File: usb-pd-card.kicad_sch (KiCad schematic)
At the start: 48 parts, among them J1 USB_C_Receptacle_USB2.0_14P, U1 CH32X035G8U6, U2 HT7533-1, U3 NT3H2111W0FHKH

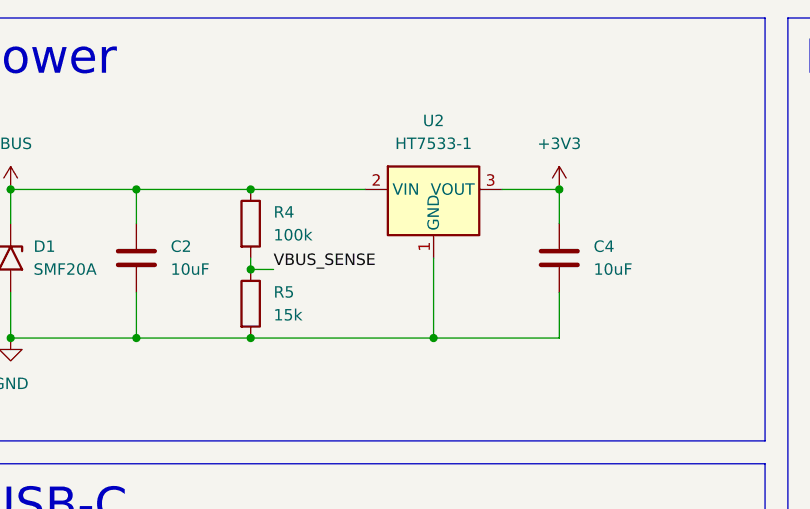
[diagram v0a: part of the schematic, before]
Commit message: v1: PCB layout complete, JLC production files
- Credit-card outline (85.6 x 53.98 mm, r3.18), USB-C paddle on the left edge
- Electronics routed, GND pour on both layers over the electronics half
- NFC coil 46 x 38 mm, 5 turns (est. 2.31 uH, f0 ~14.4 MHz), C3 DNP
- Regulator ME6228A33M3G (SOT-23-3), C2 0603, D1 SOD-123F footprint
- Contact info + QR code on the back, LED/test-pad labels on the front
- tools/nfc_coil.py coil generator and lib/nfc-coils.pretty footprint
- JLCPCB Gerbers, BOM and CPL in jlcpcb/
- README with board renders; AGENTS.md updated with final decisions
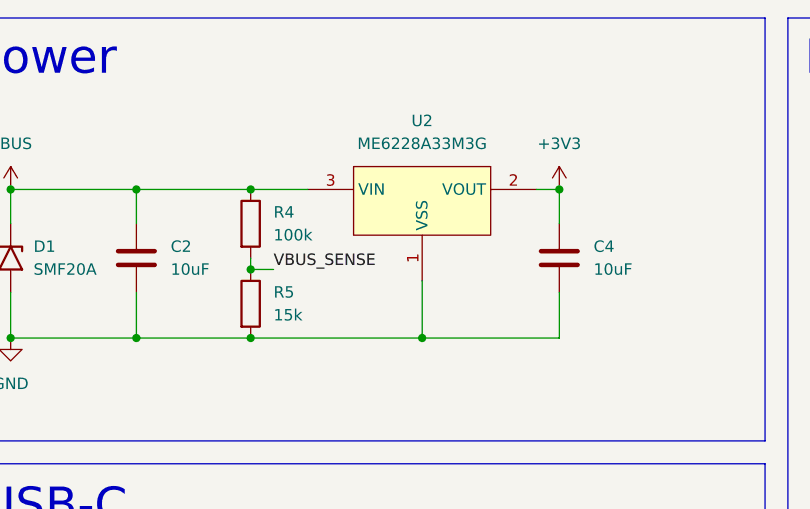
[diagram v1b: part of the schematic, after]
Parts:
- C2: footprint Capacitor_SMD:C_0805_2012Metric -> Capacitor_SMD:C_0603_1608Metric; LCSC C15850 -> C96446
- D1: footprint Diode_SMD:D_SMF -> Diode_SMD:D_SOD-123F
- L1: footprint (none) -> nfc-coils:NFC_Coil_Rect_38x46mm_R4_5T_W0.5_S0.3
- U2: value HT7533-1 -> ME6228A33M3G; footprint Package_TO_SOT_SMD:SOT-89-3 -> business-card:SOT-23-3_L2.9-W1.6-P1.90-LS2.8-BR; symbol Regulator_Linear:HT75xx-1-SOT89 -> business-card:ME6228A33M3G; LCSC C14289 -> C487914; MPN (none) -> ME6228A33M3G; Manufacturer (none) -> MICRONE(南京微盟)
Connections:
- net +3V3: now also U2.2 (VOUT); no longer U2.3 (VOUT)
- net VBUS: now also U2.3 (VIN); no longer U2.2 (VIN)
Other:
- moved on the sheet: U2
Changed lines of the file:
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@@
 	)
 	(junction
-		(at 152.4 34.29)
-		(diameter 0)
-		(color 0 0 0 0)
-	)
-	(junction
 		(at 101.6 123.19)
 		(diameter 0)
@@
 	)
 	(junction
-		(at 138.43 50.8)
+		(at 133.35 91.44)
 		(diameter 0)
 		(color 0 0 0 0)
 	)
 	(junction
-		(at 133.35 91.44)
+		(at 152.4 34.29)
 		(diameter 0)
 		(color 0 0 0 0)
@@
 	)
 	(junction
-		(at 118.11 34.29)
-		(diameter 0)
-		(color 0 0 0 0)
-	)
-	(junction
 		(at 266.7 68.58)
 		(diameter 0)
@@
 	)
 	(junction
+		(at 137.16 50.8)
+		(diameter 0)
+		(color 0 0 0 0)
+	)
+	(junction
 		(at 229.87 105.41)
 		(diameter 0)
@@
 	)
 	(junction
+		(at 118.11 34.29)
+		(diameter 0)
+		(color 0 0 0 0)
+	)
+	(junction
 		(at 123.19 91.44)
 		(diameter 0)
@@
 	(wire
 		(pts
+			(xy 118.11 34.29) (xy 124.46 34.29)
+		)
+		(stroke
+			(width 0)
+			(type default)
+		)
+	)
+	(wire
+		(pts
 			(xy 118.11 41.91) (xy 118.11 43.18)
 		)
@@
 	(wire
 		(pts
-			(xy 118.11 34.29) (xy 130.81 34.29)
+			(xy 245.11 43.18) (xy 248.92 43.18)
 		)
 		(stroke
@@
 	(wire
 		(pts
-			(xy 146.05 34.29) (xy 152.4 34.29)
+			(xy 210.82 53.34) (xy 214.63 53.34)
 		)
 		(stroke
@@
 	(wire
 		(pts
-			(xy 245.11 43.18) (xy 248.92 43.18)
+			(xy 118.11 43.18) (xy 120.65 43.18)
 		)
 		(stroke
@@
 	(wire
 		(pts
-			(xy 210.82 53.34) (xy 214.63 53.34)
+			(xy 57.15 60.96) (xy 59.69 60.96)
 		)
 		(stroke
@@
 	(wire
 		(pts
-			(xy 118.11 43.18) (xy 120.65 43.18)
+			(xy 266.7 50.8) (xy 266.7 53.34)
 		)
 		(stroke
@@
 	(wire
 		(pts
-			(xy 57.15 60.96) (xy 59.69 60.96)
+			(xy 229.87 24.13) (xy 238.76 24.13)
 		)
 		(stroke
@@
 	(wire
 		(pts
-			(xy 266.7 50.8) (xy 266.7 53.34)
+			(xy 186.69 48.26) (xy 214.63 48.26)
 		)
 		(stroke
@@
 	(wire
 		(pts
-			(xy 229.87 24.13) (xy 238.76 24.13)
+			(xy 116.84 83.82) (xy 132.08 83.82)
 		)
 		(stroke
@@
 	(wire
 		(pts
-			(xy 186.69 48.26) (xy 214.63 48.26)
+			(xy 149.86 34.29) (xy 152.4 34.29)
 		)
 		(stroke
@@
 	(wire
 		(pts
-			(xy 116.84 83.82) (xy 132.08 83.82)
+			(xy 123.19 91.44) (xy 133.35 91.44)
 		)
 		(stroke
@@
 	(wire
 		(pts
-			(xy 123.19 91.44) (xy 133.35 91.44)
+			(xy 152.4 34.29) (xy 152.4 38.1)
 		)
 		(stroke
@@
 	(wire
 		(pts
-			(xy 152.4 34.29) (xy 152.4 38.1)
+			(xy 137.16 50.8) (xy 152.4 50.8)
 		)
 		(stroke
@@
 	(wire
 		(pts
+			(xy 137.16 44.45) (xy 137.16 50.8)
+		)
+		(stroke
+			(width 0)
+			(type default)
+		)
+	)
+	(wire
+		(pts
 			(xy 256.54 50.8) (xy 259.08 50.8)
 		)
@@
 	(wire
 		(pts
-			(xy 138.43 50.8) (xy 118.11 50.8)
+			(xy 118.11 50.8) (xy 137.16 50.8)
 		)
 		(stroke
@@
 	(wire
 		(pts
-			(xy 152.4 50.8) (xy 138.43 50.8)
-		)
-		(stroke
-			(width 0)
-			(type default)
-		)
-	)
-	(wire
-		(pts
 			(xy 256.54 76.2) (xy 259.08 76.2)
 		)
@@
 	(wire
 		(pts
-			(xy 138.43 41.91) (xy 138.43 50.8)
-		)
-		(stroke
-			(width 0)
-			(type default)
-		)
-	)
-	(wire
-		(pts
 			(xy 229.87 99.06) (xy 229.87 106.68)
 		)
@@
 	)
 	(symbol
-		(lib_id "Regulator_Linear:HT75xx-1-SOT89")
-		(at 138.43 36.83 0)
+		(lib_id "business-card:ME6228A33M3G")
+		(at 137.16 38.1 0)
 		(unit 1)
 		(body_style 1)
@@
 		(fields_autoplaced yes)
 		(property "Reference" "U2"
-			(at 138.43 26.67 0)
+			(at 137.16 26.67 0)
 			(show_name no)
 			(do_not_autoplace no)
@@
 			)
 		)
-		(property "Value" "HT7533-1"
-			(at 138.43 29.21 0)
+		(property "Value" "ME6228A33M3G"
+			(at 137.16 29.21 0)
 			(show_name no)
 			(do_not_autoplace no)
@@
 			)
 		)
-		(property "Footprint" "Package_TO_SOT_SMD:SOT-89-3"
-			(at 138.43 28.575 0)
+		(property "Footprint" "business-card:SOT-23-3_L2.9-W1.6-P1.90-LS2.8-BR"
+			(at 137.16 52.07 0)
 			(hide yes)
 			(show_name no)
@@
 				(font
 					(size 1.27 1.27)
-					(italic yes)
 				)
 			)
 		)
-		(property "Datasheet" "https://www.holtek.com/documents/10179/116711/HT75xx-1v250.pdf"
-			(at 138.43 34.29 0)
+		(property "Datasheet" "https://lcsc.com/product-detail/New-Arrivals_MICRONE-Nanjing-Micro-One-Elec-ME6228A33M3G_C487914.html"
+			(at 137.16 54.61 0)
 			(hide yes)
 			(show_name no)
@@
 		)
 		(property "Description" "100mA Low Dropout Voltage Regulator, Fixed Output, SOT89"
-			(at 138.43 36.83 0)
+			(at 137.16 38.1 0)
 			(hide yes)
 			(show_name no)
@@
 			)
 		)
-		(property "LCSC" "C14289"
-			(at 138.43 28.575 0)
+		(property "LCSC" "C487914"
+			(at 137.16 62.23 0)
+			(hide yes)
+			(show_name no)
+			(do_not_autoplace no)
+			(effects
+				(font
+					(size 1.27 1.27)
+				)
+			)
+		)
+		(property "Manufacturer" "MICRONE(南京微盟)"
+			(at 137.16 57.15 0)
+			(hide yes)
+			(show_name no)
+			(do_not_autoplace no)
+			(effects
+				(font
+					(size 1.27 1.27)
+				)
+			)
+		)
+		(property "MPN" "ME6228A33M3G"
+			(at 137.16 59.69 0)
 			(hide yes)
 			(show_name no)
@@
 				(font
 					(size 1.27 1.27)
-					(italic yes)
 				)
 			)
@@
 			)
 		)
-		(property "Footprint" ""
+		(property "Footprint" "nfc-coils:NFC_Coil_Rect_38x46mm_R4_5T_W0.5_S0.3"
 			(at 46.99 25.4 0)
 			(hide yes)
@@
 			)
 		)
-		(property "Footprint" "Diode_SMD:D_SMF"
+		(property "Footprint" "Diode_SMD:D_SOD-123F"
 			(at 86.36 41.91 0)
 			(hide yes)
@@
 			)
 		)
-		(property "Footprint" "Capacitor_SMD:C_0805_2012Metric"
+		(property "Footprint" "Capacitor_SMD:C_0603_1608Metric"
 			(at 106.3752 45.72 0)
 			(hide yes)
@@
 			)
 		)
-		(property "LCSC" "C15850"
+		(property "LCSC" "C96446"
 			(at 106.3752 45.72 0)
 			(hide yes)
